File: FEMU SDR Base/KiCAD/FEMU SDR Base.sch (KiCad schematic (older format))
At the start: 90 parts, among them M1 M1, M10 M1, M11 M1, M12 M1, M13 M1, M14 M1, M15 M1, M16 M1, M2 M1, M3 M1, M4 M1, M5 M1, M6 M1, M7 M1, M8 M1, M9 M1, P1 Battery, P10 PWM2, P11 PWM3, P12 PWM4, P13 PWM1, P14 PWM2, P15 PWM3, P16 PWM4, P17 12V, P18 GND, P19 12V, P2 SDR_Shield_1, P20 GND, P21 SDR0, P22 SDR1, P27 PWM0, P28 PWM5, P29 PWM6, P3 SDR_Shield_2, P30 PWM7, P31 PWM0, P32 PWM5, P33 PWM6, P34 PWM7, P35 Battery, P36 RPi, P37 PXH, P38 Rx, P4 12V, P5 GND, P6 12V, P7 GND, P8 Raspi_Power_Shield, P9 PWM1, U1 TPS562209, U2 LP38858-LDO, U3 LP38858-LDO, U4 LM1117, U5 LM1117

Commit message: Added back silkscreen, fixed issues and added mounting holes
Signed-off-by: hardiepienaar <hardiepienaar@gmail.com>
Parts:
- added M17: SMA1, Misc footprints:MountHole, symbol CONN_01X01
- added M18: SMA2, Misc footprints:MountHole, symbol CONN_01X01
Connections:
- net GND: now also M17.1 (P1), M18.1 (P1)
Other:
- note added: "SMA Mounts\n\n\n"
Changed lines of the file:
@@
 $EndComp
 $Comp
-L GND #PWR21
+L GND #PWR22
 U 1 1 572262D4
 P 6450 3250
-F 0 "#PWR21" H 6450 3000 50  0001 C CNN
+F 0 "#PWR22" H 6450 3000 50  0001 C CNN
 F 1 "GND" H 6450 3100 50  0000 C CNN
 F 2 "" H 6450 3250 50  0000 C CNN
@@
 RS stock no. 698-9044
 $Comp
-L GND #PWR23
+L GND #PWR24
 U 1 1 5728D614
 P 7950 3700
-F 0 "#PWR23" H 7950 3450 50  0001 C CNN
+F 0 "#PWR24" H 7950 3450 50  0001 C CNN
 F 1 "GND" H 7950 3550 50  0000 C CNN
 F 2 "" H 7950 3700 50  0000 C CNN
@@
 $EndComp
 $Comp
-L GND #PWR25
+L GND #PWR26
 U 1 1 5728D688
 P 9800 3450
-F 0 "#PWR25" H 9800 3200 50  0001 C CNN
+F 0 "#PWR26" H 9800 3200 50  0001 C CNN
 F 1 "GND" H 9800 3300 50  0000 C CNN
 F 2 "" H 9800 3450 50  0000 C CNN
@@
 $EndComp
 $Comp
-L GND #PWR26
+L GND #PWR27
 U 1 1 5728D6FC
 P 9800 4600
-F 0 "#PWR26" H 9800 4350 50  0001 C CNN
+F 0 "#PWR27" H 9800 4350 50  0001 C CNN
 F 1 "GND" H 9800 4450 50  0000 C CNN
 F 2 "" H 9800 4600 50  0000 C CNN
@@
 $EndComp
 $Comp
-L GND #PWR22
+L GND #PWR23
 U 1 1 5729D4BF
 P 6450 4550
-F 0 "#PWR22" H 6450 4300 50  0001 C CNN
+F 0 "#PWR23" H 6450 4300 50  0001 C CNN
 F 1 "GND" H 6450 4400 50  0000 C CNN
 F 2 "" H 6450 4550 50  0000 C CNN
@@
 $EndComp
 $Comp
-L GND #PWR24
+L GND #PWR25
 U 1 1 5735C820
 P 7950 4850
-F 0 "#PWR24" H 7950 4600 50  0001 C CNN
+F 0 "#PWR25" H 7950 4600 50  0001 C CNN
 F 1 "GND" H 7950 4700 50  0000 C CNN
 F 2 "" H 7950 4850 50  0000 C CNN
@@
 	1    0    0    -1
 $EndComp
+$Comp
+L CONN_01X01 M17
+U 1 1 57381487
+P 6150 6600
+F 0 "M17" H 6150 6700 50  0000 C CNN
+F 1 "SMA1" V 6250 6600 50  0000 C CNN
+F 2 "Misc footprints:MountHole" H 6150 6600 50  0001 C CNN
+F 3 "" H 6150 6600 50  0000 C CNN
+	1    6150 6600
+	0    -1   -1   0
+$EndComp
+$Comp
+L CONN_01X01 M18
+U 1 1 573817B2
+P 6400 6600
+F 0 "M18" H 6400 6700 50  0000 C CNN
+F 1 "SMA2" V 6500 6600 50  0000 C CNN
+F 2 "Misc footprints:MountHole" H 6400 6600 50  0001 C CNN
+F 3 "" H 6400 6600 50  0000 C CNN
+	1    6400 6600
+	0    -1   -1   0
+$EndComp
+Text Notes 6050 6600 0    60   ~ 0
+SMA Mounts\n\n\n
+$Comp
+L GND #PWR21
+U 1 1 57382131
+P 6300 6950
+F 0 "#PWR21" H 6300 6700 50  0001 C CNN
+F 1 "GND" H 6300 6800 50  0000 C CNN
+F 2 "" H 6300 6950 50  0000 C CNN
+F 3 "" H 6300 6950 50  0000 C CNN
+	1    6300 6950
+	1    0    0    -1
+$EndComp
+Wire Wire Line
+	6150 6800 6400 6800
+Wire Wire Line
+	6300 6950 6300 6800
+Connection ~ 6300 6800
 $EndSCHEMATC

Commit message: Status=Free, Ground -12V overlap fixed on power pins, stitching vias made smaller to stay within Seeed manufacturing limits, cable tray vias all connected to ground, bottom silkscreen overlap of text fixed
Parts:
- C4, C5: footprint Capacitors_SMD:C_1206_HandSoldering -> Capacitors_Tantalum_SMD:TantalC_SizeS_EIA-3216
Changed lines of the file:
@@
 F 0 "C4" H 3175 1050 50  0000 L CNN
 F 1 "33u" H 3175 850 50  0000 L CNN
-F 2 "Capacitors_SMD:C_1206_HandSoldering" H 3188 800 50  0001 C CNN
+F 2 "Capacitors_Tantalum_SMD:TantalC_SizeS_EIA-3216" H 3188 800 50  0001 C CNN
 F 3 "" H 3150 950 50  0000 C CNN
 	1    3150 950
@@
 F 0 "C5" H 3375 1050 50  0000 L CNN
 F 1 "33u" H 3375 850 50  0000 L CNN
-F 2 "Capacitors_SMD:C_1206_HandSoldering" H 3388 800 50  0001 C CNN
+F 2 "Capacitors_Tantalum_SMD:TantalC_SizeS_EIA-3216" H 3388 800 50  0001 C CNN
 F 3 "" H 3350 950 50  0000 C CNN
 	1    3350 950
@@
 $EndComp
 $Comp
-L +12V #PWR2
+L +12V #PWR01
 U 1 1 57077D61
 P 700 1600
-F 0 "#PWR2" H 700 1450 50  0001 C CNN
+F 0 "#PWR01" H 700 1450 50  0001 C CNN
 F 1 "+12V" H 700 1740 50  0000 C CNN
 F 2 "" H 700 1600 50  0000 C CNN
@@
 $EndComp
 $Comp
-L +5V #PWR9
+L +5V #PWR02
 U 1 1 57077E13
 P 3900 700
-F 0 "#PWR9" H 3900 550 50  0001 C CNN
+F 0 "#PWR02" H 3900 550 50  0001 C CNN
 F 1 "+5V" H 3900 840 50  0000 C CNN
 F 2 "" H 3900 700 50  0000 C CNN
@@
 $EndComp
 $Comp
-L +12V #PWR4
+L +12V #PWR03
 U 1 1 5722422D
 P 1900 2550
-F 0 "#PWR4" H 1900 2400 50  0001 C CNN
+F 0 "#PWR03" H 1900 2400 50  0001 C CNN
 F 1 "+12V" H 1900 2690 50  0000 C CNN
 F 2 "" H 1900 2550 50  0000 C CNN
@@
 $EndComp
 $Comp
-L GND #PWR3
+L GND #PWR04
 U 1 1 572251A0
 P 1400 6900
-F 0 "#PWR3" H 1400 6650 50  0001 C CNN
+F 0 "#PWR04" H 1400 6650 50  0001 C CNN
 F 1 "GND" H 1400 6750 50  0000 C CNN
 F 2 "" H 1400 6900 50  0000 C CNN
@@
 $EndComp
 $Comp
-L GND #PWR5
+L GND #PWR05
 U 1 1 57225200
 P 2000 6900
-F 0 "#PWR5" H 2000 6650 50  0001 C CNN
+F 0 "#PWR05" H 2000 6650 50  0001 C CNN
 F 1 "GND" H 2000 6750 50  0000 C CNN
 F 2 "" H 2000 6900 50  0000 C CNN
@@
 $EndComp
 $Comp
-L GND #PWR7
+L GND #PWR06
 U 1 1 57225259
 P 2700 6900
-F 0 "#PWR7" H 2700 6650 50  0001 C CNN
+F 0 "#PWR06" H 2700 6650 50  0001 C CNN
 F 1 "GND" H 2700 6750 50  0000 C CNN
 F 2 "" H 2700 6900 50  0000 C CNN
@@
 $EndComp
 $Comp
-L GND #PWR22
+L GND #PWR07
 U 1 1 572262D4
 P 6450 3250
-F 0 "#PWR22" H 6450 3000 50  0001 C CNN
+F 0 "#PWR07" H 6450 3000 50  0001 C CNN
 F 1 "GND" H 6450 3100 50  0000 C CNN
 F 2 "" H 6450 3250 50  0000 C CNN
@@
 $EndComp
 $Comp
-L +5V #PWR19
+L +5V #PWR08
 U 1 1 572267F7
 P 5600 2600
-F 0 "#PWR19" H 5600 2450 50  0001 C CNN
+F 0 "#PWR08" H 5600 2450 50  0001 C CNN
 F 1 "+5V" H 5600 2740 50  0000 C CNN
 F 2 "" H 5600 2600 50  0000 C CNN
@@
 RS stock no. 698-9044
 $Comp
-L GND #PWR24
+L GND #PWR09
 U 1 1 5728D614
 P 7950 3700
-F 0 "#PWR24" H 7950 3450 50  0001 C CNN
+F 0 "#PWR09" H 7950 3450 50  0001 C CNN
 F 1 "GND" H 7950 3550 50  0000 C CNN
 F 2 "" H 7950 3700 50  0000 C CNN
@@
 $EndComp
 $Comp
-L GND #PWR26
+L GND #PWR010
 U 1 1 5728D688
 P 9800 3450
-F 0 "#PWR26" H 9800 3200 50  0001 C CNN
+F 0 "#PWR010" H 9800 3200 50  0001 C CNN
 F 1 "GND" H 9800 3300 50  0000 C CNN
 F 2 "" H 9800 3450 50  0000 C CNN
@@
 $EndComp
 $Comp
-L GND #PWR27
+L GND #PWR011
 U 1 1 5728D6FC
 P 9800 4600
-F 0 "#PWR27" H 9800 4350 50  0001 C CNN
+F 0 "#PWR011" H 9800 4350 50  0001 C CNN
 F 1 "GND" H 9800 4450 50  0000 C CNN
 F 2 "" H 9800 4600 50  0000 C CNN
@@
 $EndComp
 $Comp
-L GND #PWR23
+L GND #PWR012
 U 1 1 5729D4BF
 P 6450 4550
-F 0 "#PWR23" H 6450 4300 50  0001 C CNN
+F 0 "#PWR012" H 6450 4300 50  0001 C CNN
 F 1 "GND" H 6450 4400 50  0000 C CNN
 F 2 "" H 6450 4550 50  0000 C CNN
@@
 $EndComp
 $Comp
-L GND #PWR8
+L GND #PWR013
 U 1 1 5734751C
 P 3250 1350
-F 0 "#PWR8" H 3250 1100 50  0001 C CNN
+F 0 "#PWR013" H 3250 1100 50  0001 C CNN
 F 1 "GND" H 3250 1200 50  0000 C CNN
 F 2 "" H 3250 1350 50  0000 C CNN
@@
 $EndComp
 $Comp
-L GND #PWR1
+L GND #PWR014
 U 1 1 57347B92
 P 650 1150
-F 0 "#PWR1" H 650 900 50  0001 C CNN
+F 0 "#PWR014" H 650 900 50  0001 C CNN
 F 1 "GND" H 650 1000 50  0000 C CNN
 F 2 "" H 650 1150 50  0000 C CNN
@@
 $EndComp
 $Comp
-L GND #PWR6
+L GND #PWR015
 U 1 1 5734BB86
 P 2100 2650
-F 0 "#PWR6" H 2100 2400 50  0001 C CNN
+F 0 "#PWR015" H 2100 2400 50  0001 C CNN
 F 1 "GND" H 2100 2500 50  0000 C CNN
 F 2 "" H 2100 2650 50  0000 C CNN
@@
 $EndComp
 $Comp
-L GND #PWR25
+L GND #PWR016
 U 1 1 5735C820
 P 7950 4850
-F 0 "#PWR25" H 7950 4600 50  0001 C CNN
+F 0 "#PWR016" H 7950 4600 50  0001 C CNN
 F 1 "GND" H 7950 4700 50  0000 C CNN
 F 2 "" H 7950 4850 50  0000 C CNN
@@
 $EndComp
 $Comp
-L GND #PWR10
+L GND #PWR017
 U 1 1 5736D6EB
 P 3950 6850
-F 0 "#PWR10" H 3950 6600 50  0001 C CNN
+F 0 "#PWR017" H 3950 6600 50  0001 C CNN
 F 1 "GND" H 3950 6700 50  0000 C CNN
 F 2 "" H 3950 6850 50  0000 C CNN
@@
 $EndComp
 $Comp
-L GND #PWR15
+L GND #PWR018
 U 1 1 57371837
 P 4700 6100
-F 0 "#PWR15" H 4700 5850 50  0001 C CNN
+F 0 "#PWR018" H 4700 5850 50  0001 C CNN
 F 1 "GND" H 4700 5950 50  0000 C CNN
 F 2 "" H 4700 6100 50  0000 C CNN
@@
 $EndComp
 $Comp
-L GND #PWR14
+L GND #PWR019
 U 1 1 57371E72
 P 4700 5750
-F 0 "#PWR14" H 4700 5500 50  0001 C CNN
+F 0 "#PWR019" H 4700 5500 50  0001 C CNN
 F 1 "GND" H 4700 5600 50  0000 C CNN
 F 2 "" H 4700 5750 50  0000 C CNN
@@
 $EndComp
 $Comp
-L GND #PWR13
+L GND #PWR020
 U 1 1 57371F85
 P 4700 5400
-F 0 "#PWR13" H 4700 5150 50  0001 C CNN
+F 0 "#PWR020" H 4700 5150 50  0001 C CNN
 F 1 "GND" H 4700 5250 50  0000 C CNN
 F 2 "" H 4700 5400 50  0000 C CNN
@@
 $EndComp
 $Comp
-L +5V #PWR16
+L +5V #PWR021
 U 1 1 573725CA
 P 4850 5300
-F 0 "#PWR16" H 4850 5150 50  0001 C CNN
+F 0 "#PWR021" H 4850 5150 50  0001 C CNN
 F 1 "+5V" H 4850 5440 50  0000 C CNN
 F 2 "" H 4850 5300 50  0000 C CNN
@@
 $EndComp
 $Comp
-L +5V #PWR17
+L +5V #PWR022
 U 1 1 57372D65
 P 4850 5650
-F 0 "#PWR17" H 4850 5500 50  0001 C CNN
+F 0 "#PWR022" H 4850 5500 50  0001 C CNN
 F 1 "+5V" H 4850 5790 50  0000 C CNN
 F 2 "" H 4850 5650 50  0000 C CNN
@@
 $EndComp
 $Comp
-L +5V #PWR18
+L +5V #PWR023
 U 1 1 57372E78
 P 4850 6000
-F 0 "#PWR18" H 4850 5850 50  0001 C CNN
+F 0 "#PWR023" H 4850 5850 50  0001 C CNN
 F 1 "+5V" H 4850 6140 50  0000 C CNN
 F 2 "" H 4850 6000 50  0000 C CNN
@@
 	4650 3300 4300 3300
 $Comp
-L GND #PWR12
+L GND #PWR024
 U 1 1 573735FD
 P 4500 3100
-F 0 "#PWR12" H 4500 2850 50  0001 C CNN
+F 0 "#PWR024" H 4500 2850 50  0001 C CNN
 F 1 "GND" H 4500 2950 50  0000 C CNN
 F 2 "" H 4500 3100 50  0000 C CNN
@@
 $EndComp
 $Comp
-L GND #PWR11
+L GND #PWR025
 U 1 1 5737370A
 P 4500 2550
-F 0 "#PWR11" H 4500 2300 50  0001 C CNN
+F 0 "#PWR025" H 4500 2300 50  0001 C CNN
 F 1 "GND" H 4500 2400 50  0000 C CNN
 F 2 "" H 4500 2550 50  0000 C CNN
@@
 $EndComp
 $Comp
-L +5V #PWR20
+L +5V #PWR026
 U 1 1 573755E8
 P 5600 3900
-F 0 "#PWR20" H 5600 3750 50  0001 C CNN
+F 0 "#PWR026" H 5600 3750 50  0001 C CNN
 F 1 "+5V" H 5600 4040 50  0000 C CNN
 F 2 "" H 5600 3900 50  0000 C CNN
@@
 SMA Mounts\n\n\n
 $Comp
-L GND #PWR21
+L GND #PWR027
 U 1 1 57382131
 P 6300 6950
-F 0 "#PWR21" H 6300 6700 50  0001 C CNN
+F 0 "#PWR027" H 6300 6700 50  0001 C CNN
 F 1 "GND" H 6300 6800 50  0000 C CNN
 F 2 "" H 6300 6950 50  0000 C CNN

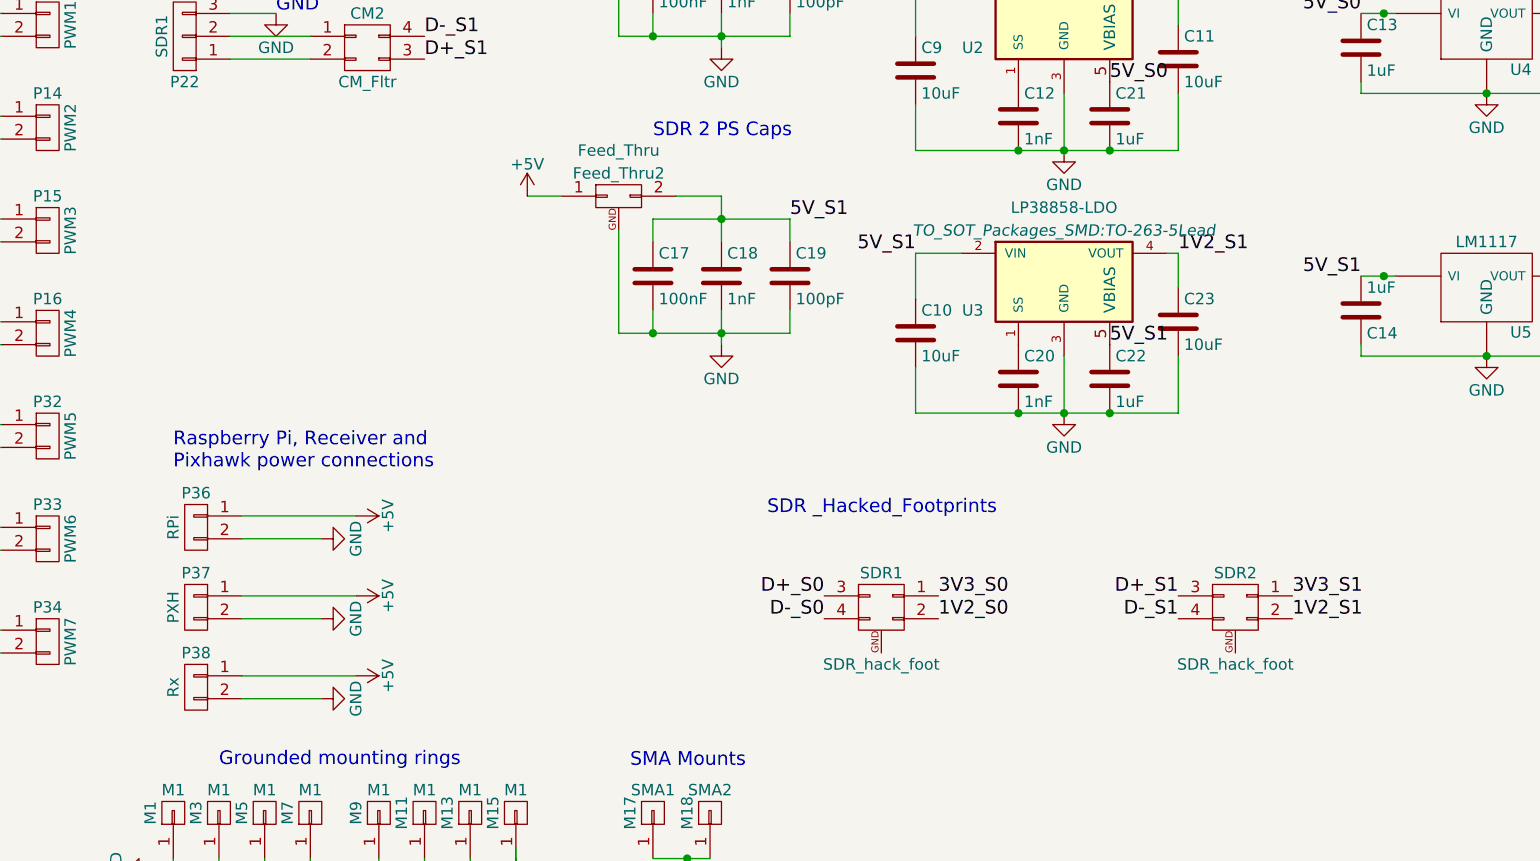
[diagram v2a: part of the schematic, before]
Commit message: saving progress while separating GND and PWR GND vias
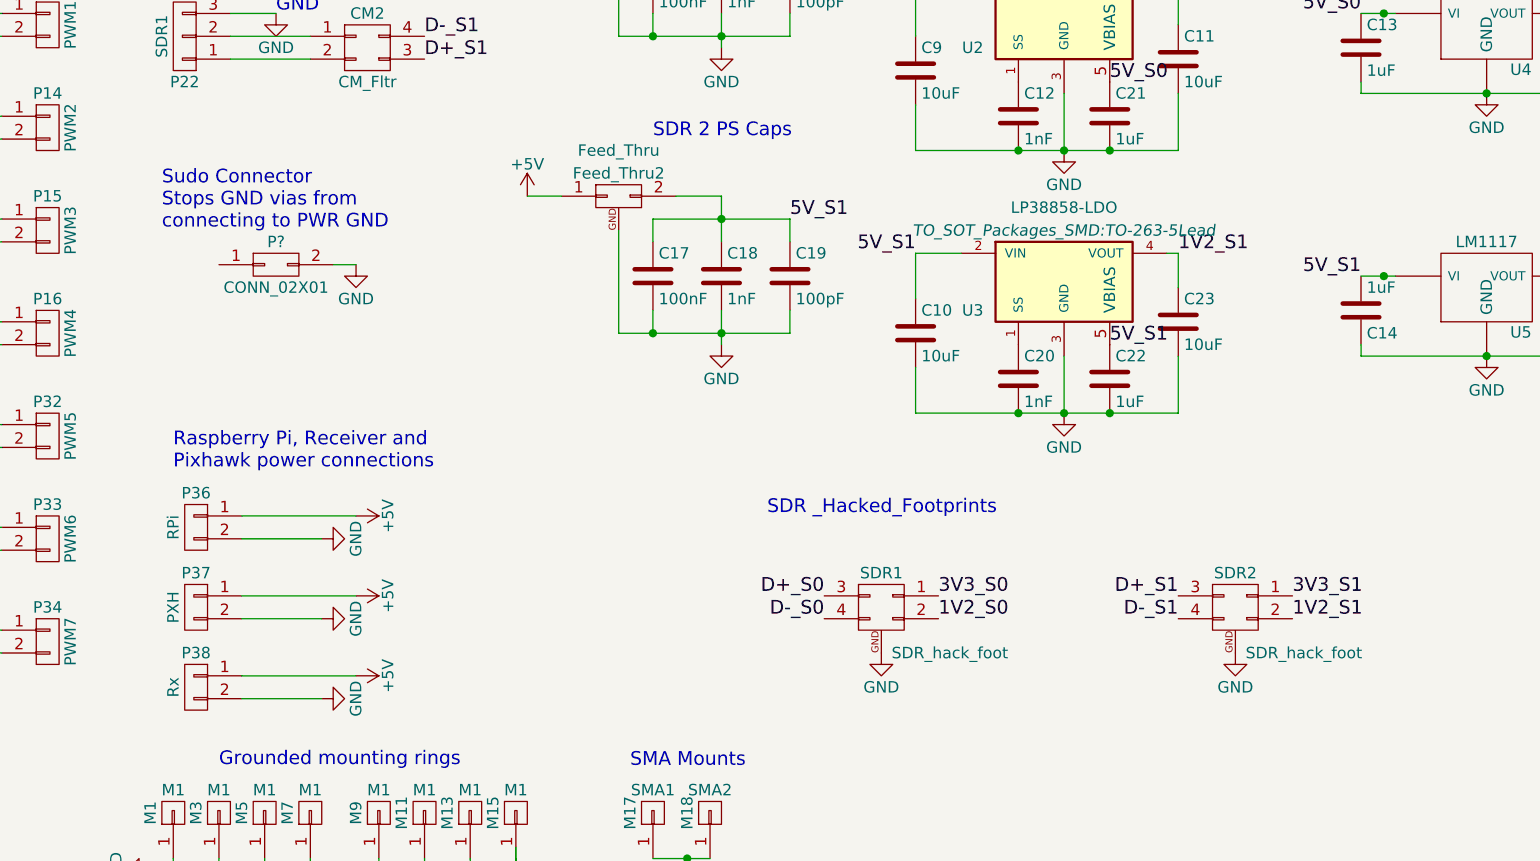
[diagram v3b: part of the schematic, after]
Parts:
- added P?: CONN_02X01, symbol CONN_02X01
- C10, C11, C12, C13, C14, C15, C16, C20, C21, C22, C9: footprint Capacitors_SMD:C_0805_HandSoldering -> Capacitors_SMD:C_0603_HandSoldering
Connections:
- net GND: now also SDR1.GND, SDR2.GND, P?.2 (P2)
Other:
- note added: "Sudo Connector\nStops GND vias from \nconnecting to PWR GND"
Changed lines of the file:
@@
 F 0 "C9" H 7325 3450 50  0000 L CNN
 F 1 "10uF" H 7325 3250 50  0000 L CNN
-F 2 "Capacitors_SMD:C_0805_HandSoldering" H 7338 3200 50  0001 C CNN
+F 2 "Capacitors_SMD:C_0603_HandSoldering" H 7338 3200 50  0001 C CNN
 F 3 "" H 7300 3350 50  0000 C CNN
 	1    7300 3350
@@
 F 0 "C11" H 8475 3400 50  0000 L CNN
 F 1 "10uF" H 8475 3200 50  0000 L CNN
-F 2 "Capacitors_SMD:C_0805_HandSoldering" H 8488 3150 50  0001 C CNN
+F 2 "Capacitors_SMD:C_0603_HandSoldering" H 8488 3150 50  0001 C CNN
 F 3 "" H 8450 3300 50  0000 C CNN
 	1    8450 3300
@@
 F 0 "C15" H 10375 3350 50  0000 L CNN
 F 1 "1uF" H 10375 3150 50  0000 L CNN
-F 2 "Capacitors_SMD:C_0805_HandSoldering" H 10388 3100 50  0001 C CNN
+F 2 "Capacitors_SMD:C_0603_HandSoldering" H 10388 3100 50  0001 C CNN
 F 3 "" H 10350 3250 50  0000 C CNN
 	1    10350 3250
@@
 F 0 "C16" H 10375 4500 50  0000 L CNN
 F 1 "1uF" H 10375 4300 50  0000 L CNN
-F 2 "Capacitors_SMD:C_0805_HandSoldering" H 10388 4250 50  0001 C CNN
+F 2 "Capacitors_SMD:C_0603_HandSoldering" H 10388 4250 50  0001 C CNN
 F 3 "" H 10350 4400 50  0000 C CNN
 	1    10350 4400
@@
 F 0 "C21" H 8175 3650 50  0000 L CNN
 F 1 "1uF" H 8175 3450 50  0000 L CNN
-F 2 "Capacitors_SMD:C_0805_HandSoldering" H 8188 3400 50  0001 C CNN
+F 2 "Capacitors_SMD:C_0603_HandSoldering" H 8188 3400 50  0001 C CNN
 F 3 "" H 8150 3550 50  0000 C CNN
 	1    8150 3550
@@
 F 0 "C12" H 7775 3650 50  0000 L CNN
 F 1 "1nF" H 7775 3450 50  0000 L CNN
-F 2 "Capacitors_SMD:C_0805_HandSoldering" H 7788 3400 50  0001 C CNN
+F 2 "Capacitors_SMD:C_0603_HandSoldering" H 7788 3400 50  0001 C CNN
 F 3 "" H 7750 3550 50  0000 C CNN
 	1    7750 3550
@@
 F 0 "C10" H 7325 4600 50  0000 L CNN
 F 1 "10uF" H 7325 4400 50  0000 L CNN
-F 2 "Capacitors_SMD:C_0805_HandSoldering" H 7338 4350 50  0001 C CNN
+F 2 "Capacitors_SMD:C_0603_HandSoldering" H 7338 4350 50  0001 C CNN
 F 3 "" H 7300 4500 50  0000 C CNN
 	1    7300 4500
@@
 F 0 "C22" H 8175 4800 50  0000 L CNN
 F 1 "1uF" H 8175 4600 50  0000 L CNN
-F 2 "Capacitors_SMD:C_0805_HandSoldering" H 8188 4550 50  0001 C CNN
+F 2 "Capacitors_SMD:C_0603_HandSoldering" H 8188 4550 50  0001 C CNN
 F 3 "" H 8150 4700 50  0000 C CNN
 	1    8150 4700
@@
 F 0 "C20" H 7775 4800 50  0000 L CNN
 F 1 "1nF" H 7775 4600 50  0000 L CNN
-F 2 "Capacitors_SMD:C_0805_HandSoldering" H 7788 4550 50  0001 C CNN
+F 2 "Capacitors_SMD:C_0603_HandSoldering" H 7788 4550 50  0001 C CNN
 F 3 "" H 7750 4700 50  0000 C CNN
 	1    7750 4700
@@
 P 7150 5700
 F 0 "SDR1" H 7150 5850 50  0000 C CNN
-F 1 "SDR_hack_foot" H 7150 5450 50  0000 C CNN
+F 1 "SDR_hack_foot" H 7450 5500 50  0000 C CNN
 F 2 "ARB_foots:SDR_hack_outline" H 7150 4500 50  0001 C CNN
 F 3 "" H 7150 4500 50  0000 C CNN
@@
 P 8700 5700
 F 0 "SDR2" H 8700 5850 50  0000 C CNN
-F 1 "SDR_hack_foot" H 8700 5450 50  0000 C CNN
+F 1 "SDR_hack_foot" H 9000 5500 50  0000 C CNN
 F 2 "ARB_foots:SDR_hack_outline" H 8700 4500 50  0001 C CNN
 F 3 "" H 8700 4500 50  0000 C CNN
@@
 F 0 "C14" H 9275 4500 50  0000 L CNN
 F 1 "1uF" H 9275 4300 50  0000 L CNN
-F 2 "Capacitors_SMD:C_0805_HandSoldering" H 9288 4250 50  0001 C CNN
+F 2 "Capacitors_SMD:C_0603_HandSoldering" H 9288 4250 50  0001 C CNN
 F 3 "" H 9250 4400 50  0000 C CNN
 	1    9250 4400
@@
 F 0 "C13" H 9275 3350 50  0000 L CNN
 F 1 "1uF" H 9275 3150 50  0000 L CNN
-F 2 "Capacitors_SMD:C_0805_HandSoldering" H 9288 3100 50  0001 C CNN
+F 2 "Capacitors_SMD:C_0603_HandSoldering" H 9288 3100 50  0001 C CNN
 F 3 "" H 9250 3250 50  0000 C CNN
 	1    9250 3250
@@
 	6300 6950 6300 6800
 Connection ~ 6300 6800
+$Comp
+L GND #PWR028
+U 1 1 573E7981
+P 7150 5900
+F 0 "#PWR028" H 7150 5650 50  0001 C CNN
+F 1 "GND" H 7150 5750 50  0000 C CNN
+F 2 "" H 7150 5900 50  0000 C CNN
+F 3 "" H 7150 5900 50  0000 C CNN
+	1    7150 5900
+	1    0    0    -1
+$EndComp
+$Comp
+L GND #PWR029
+U 1 1 573E7BBE
+P 8700 5900
+F 0 "#PWR029" H 8700 5650 50  0001 C CNN
+F 1 "GND" H 8700 5750 50  0000 C CNN
+F 2 "" H 8700 5900 50  0000 C CNN
+F 3 "" H 8700 5900 50  0000 C CNN
+	1    8700 5900
+	1    0    0    -1
+$EndComp
+$Comp
+L CONN_02X01 P?
+U 1 1 573F1A94
+P 4500 4200
+F 0 "P?" H 4500 4300 50  0000 C CNN
+F 1 "CONN_02X01" H 4500 4100 50  0000 C CNN
+F 2 "" H 4500 3000 50  0000 C CNN
+F 3 "" H 4500 3000 50  0000 C CNN
+	1    4500 4200
+	1    0    0    -1
+$EndComp
+Text Notes 4000 4050 0    60   ~ 0
+Sudo Connector\nStops GND vias from \nconnecting to PWR GND
+$Comp
+L GND #PWR?
+U 1 1 573F2142
+P 4850 4200
+F 0 "#PWR?" H 4850 3950 50  0001 C CNN
+F 1 "GND" H 4850 4050 50  0000 C CNN
+F 2 "" H 4850 4200 50  0000 C CNN
+F 3 "" H 4850 4200 50  0000 C CNN
+	1    4850 4200
+	1    0    0    -1
+$EndComp
+Wire Wire Line
+	4850 4200 4750 4200
 $EndSCHEMATC
